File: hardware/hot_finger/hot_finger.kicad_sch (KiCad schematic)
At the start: 34 parts, among them J1 USB_C_Receptacle_USB2.0, Q1 2N7002, Q2 2N7002, Q3 2N7002, Q4 2N7002, Q5 2N7002, Q6 2N7002, Q7 2N7002, Q8 2N7002, U1 RP2040

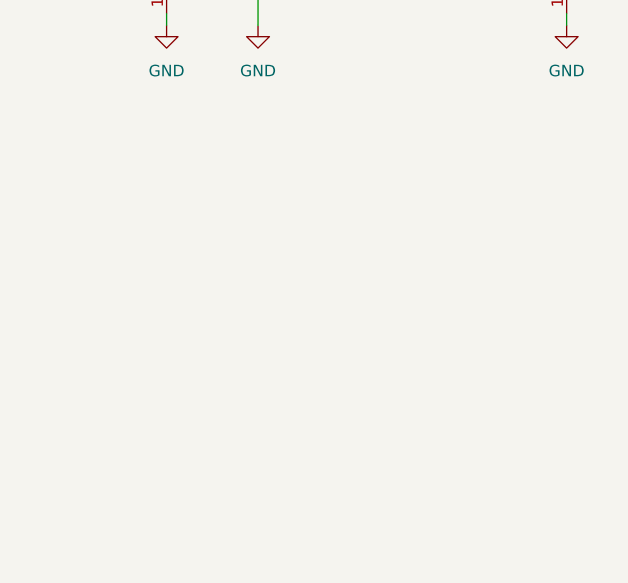
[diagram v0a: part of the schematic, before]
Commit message: feature: add photodiodes
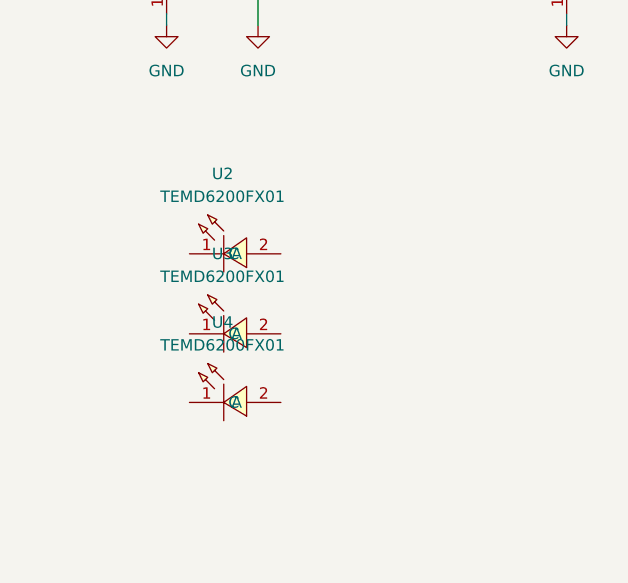
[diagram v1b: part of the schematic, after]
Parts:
- added U2, U3, U4: TEMD6200FX01, easyeda2kicad:OPTO-SMD_L2.0-W1.3-RD-1, symbol easyeda2kicad:TEMD6200FX01
